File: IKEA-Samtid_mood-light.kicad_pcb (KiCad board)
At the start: 2 copper layers, 100 x 100 mm, 156 parts, among them IC1 ATMEGA168PA-M, P1 FTDI, P2 POWER, P3.1 B-to-B-1A, P3.2 B-to-B-1B, P4.1 B-to-B-2A, P4.2 B-to-B-2B, Q1 BSS138, Q2 BSS138, SW1 ENTER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

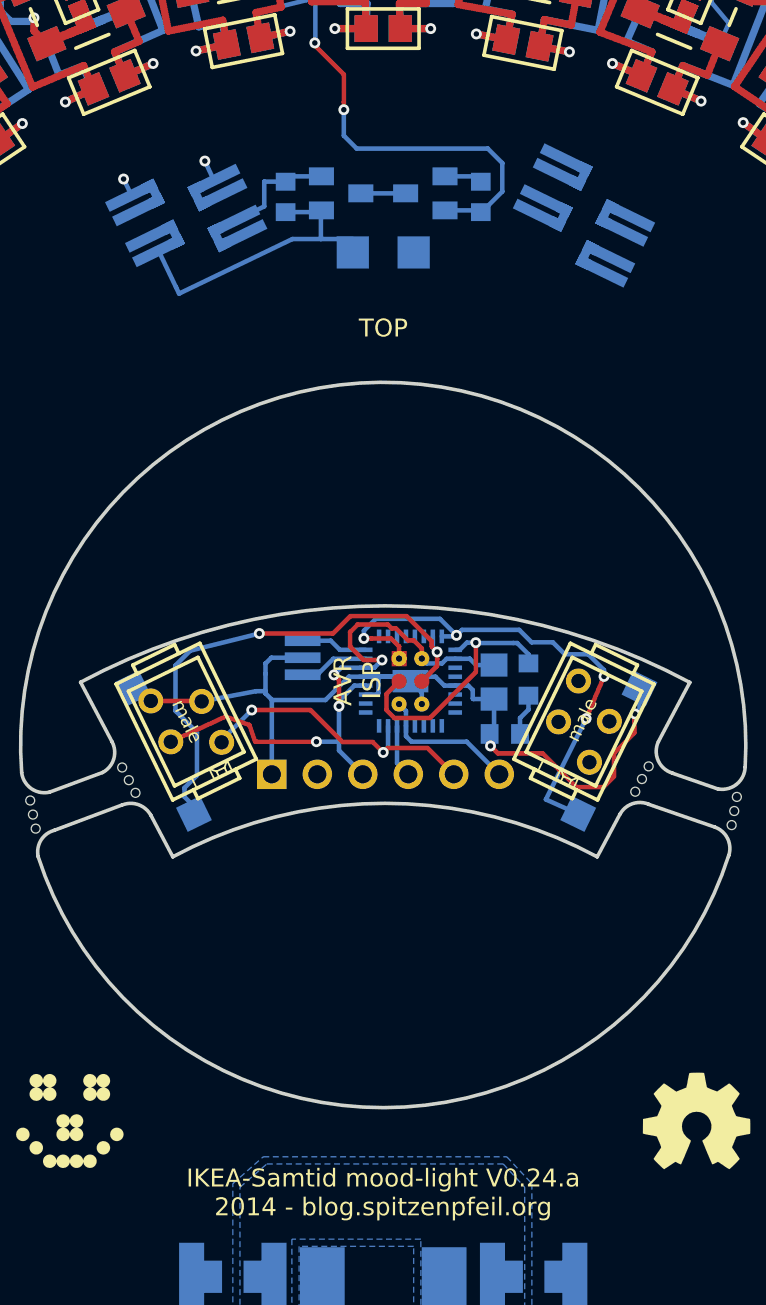
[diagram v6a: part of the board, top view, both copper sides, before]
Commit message: Changed SOT23 MOSFET footprints: D-S bridgeable.
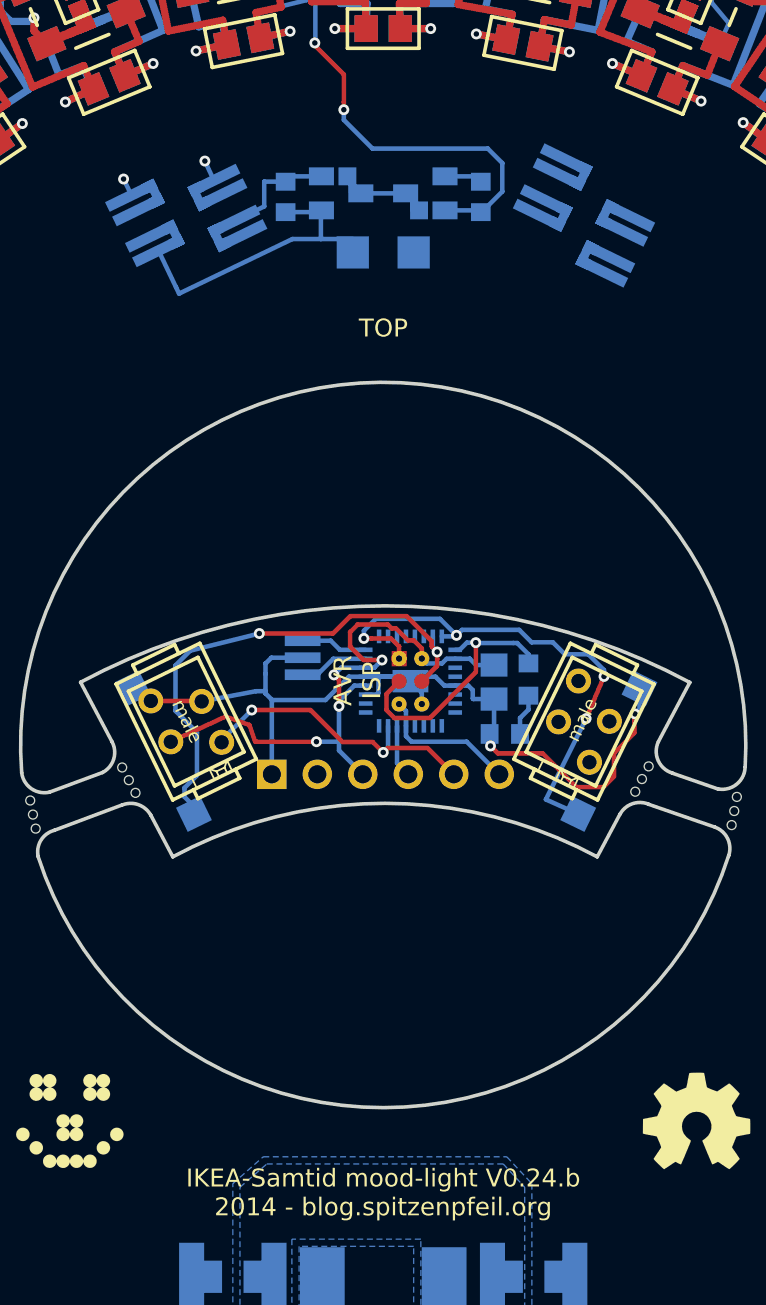
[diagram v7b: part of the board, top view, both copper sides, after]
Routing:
- net /WS2812B-LEDs-1/A_IN: track 29.4 -> 28.9 mm
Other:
- board text added: "IKEA-Samtid mood-light V0.24.b 2014 - blog.spitzenpfeil.org"
- board text removed: "IKEA-Samtid mood-light V0.24.a 2014 - blog.spitzenpfeil.org"

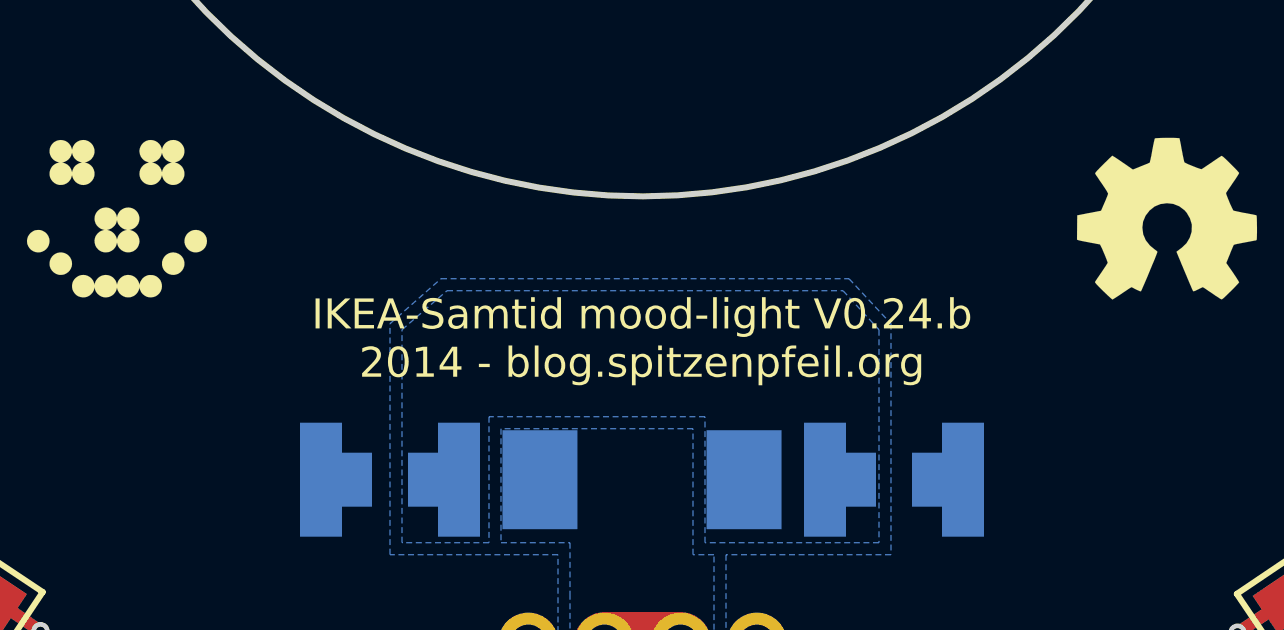
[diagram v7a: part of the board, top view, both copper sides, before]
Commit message: A bit more copper-pour pullback from the center hole.
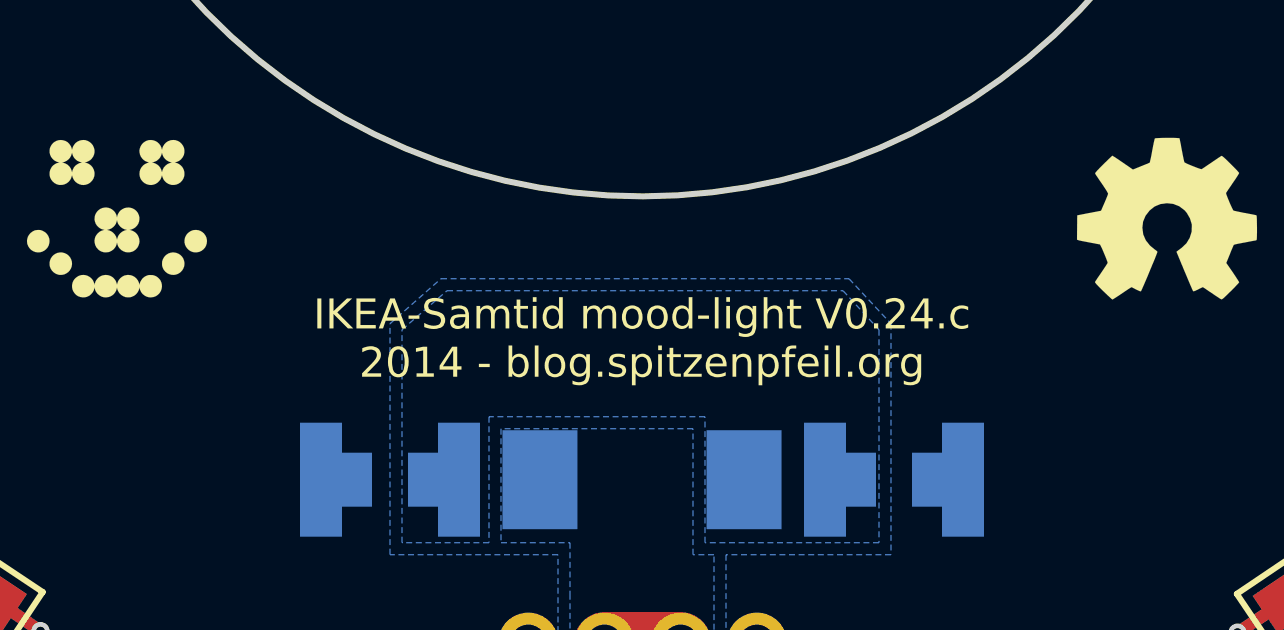
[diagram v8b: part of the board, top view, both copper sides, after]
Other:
- board text added: "IKEA-Samtid mood-light V0.24.c 2014 - blog.spitzenpfeil.org"
- board text removed: "IKEA-Samtid mood-light V0.24.b 2014 - blog.spitzenpfeil.org"
